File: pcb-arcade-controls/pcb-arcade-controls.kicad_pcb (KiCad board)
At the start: 4 copper layers, 38.1 x 57.2 mm, 26 parts, among them J1 USB_C, SW1 SW_Push, U1 STM32F072CBT6, U3 XC6206, U4 USBLC6-2SC6

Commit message: start aan pcb
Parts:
- removed REF** (x6): MX_1.00u_PG151101S11, ScottoKeebs_Scotto:MX_Hotswap_1.00u
- moved C9 16.1 mm to (156.2, 78.9)
- moved R1 16.1 mm to (142.5, 75.1)
- moved SW1 16.1 mm to (147.3, 76.5)
- moved U3 16.1 mm to (156.7, 76.4)
- moved J1 16.1 mm to (153.8, 57.3)
- moved R2 16.1 mm to (151.9, 63.9)
- moved R3 16.1 mm to (155.5, 63.8)
- moved C8 16.1 mm to (157.2, 74.0)
- moved F1 16.1 mm to (157.5, 72.7)
- moved U4 16.1 mm to (153.3, 71.4)
- moved C10 15.8 mm to (155.2, 101.6)
- moved C13 15.8 mm to (158.6, 98.2)
- moved C14 15.8 mm to (151.5, 101.6)
- moved C15 15.8 mm to (150.5, 101.6)
- moved C16 15.8 mm to (156.2, 90.8)
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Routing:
- net /BOOT0: track 34.8 -> 22.6 mm
- net +3.3V: track 71.5 -> 59.4 mm
- net /MCU_D-: track 18.6 -> 7.85 mm
- net /MCU_D+: track 18.6 -> 7.85 mm
- removed copper zone on In1.Cu, net GND
- removed copper zone on In2.Cu, net GND
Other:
- board size 38.1 x 57.2 mm -> 11 x 11 mm

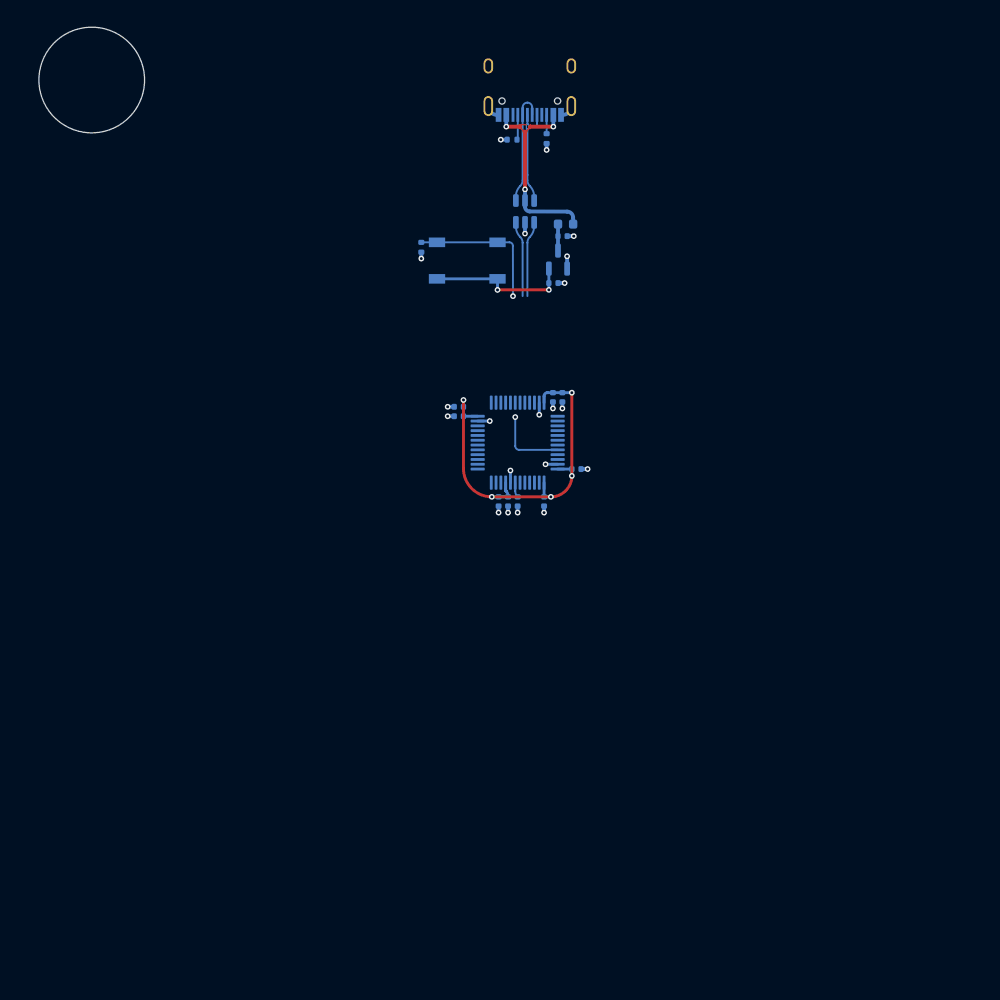
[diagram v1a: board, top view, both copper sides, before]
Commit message: PCB board wipe en connector toevoeging
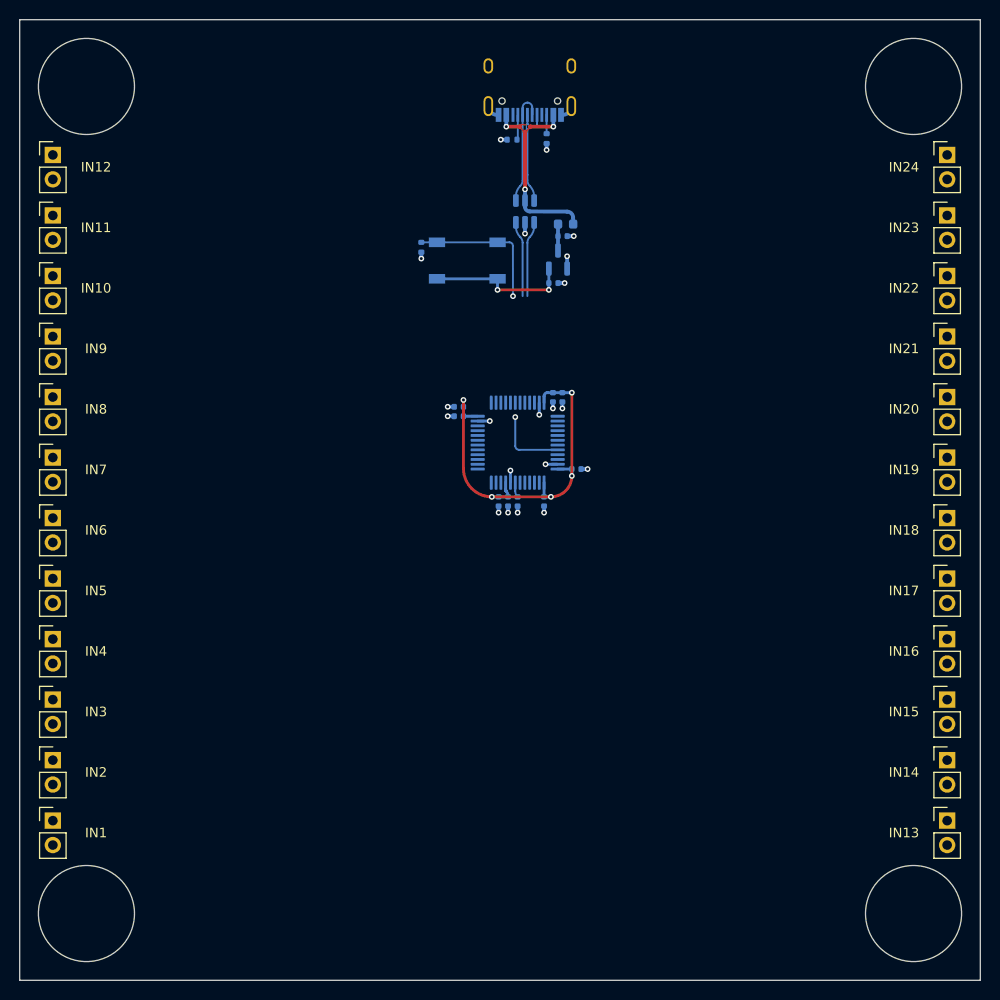
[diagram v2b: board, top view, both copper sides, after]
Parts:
- added H1: 10mm, arcade-controls:MountingHole_10mm, F.Cu at (107.6, 58.4)
- added H2: 10mm, arcade-controls:MountingHole_10mm, F.Cu at (193.7, 58.4)
- added H3: 10mm, arcade-controls:MountingHole_10mm, F.Cu at (107.6, 144.5)
- added H4: 10mm, arcade-controls:MountingHole_10mm, F.Cu at (193.7, 144.5)
- added IN1: Conn_01x02, Connector_PinHeader_2.54mm:PinHeader_1x02_P2.54mm_Vertical, F.Cu at (104.1, 134.8)
- added IN10: Conn_01x02, Connector_PinHeader_2.54mm:PinHeader_1x02_P2.54mm_Vertical, F.Cu at (104.1, 78.1)
- added IN11: Conn_01x02, Connector_PinHeader_2.54mm:PinHeader_1x02_P2.54mm_Vertical, F.Cu at (104.1, 71.8)
- added IN12: Conn_01x02, Connector_PinHeader_2.54mm:PinHeader_1x02_P2.54mm_Vertical, F.Cu at (104.1, 65.5)
- added IN13: Conn_01x02, Connector_PinHeader_2.54mm:PinHeader_1x02_P2.54mm_Vertical, F.Cu at (197.2, 134.8)
- added IN14: Conn_01x02, Connector_PinHeader_2.54mm:PinHeader_1x02_P2.54mm_Vertical, F.Cu at (197.2, 128.5)
- added IN15: Conn_01x02, Connector_PinHeader_2.54mm:PinHeader_1x02_P2.54mm_Vertical, F.Cu at (197.2, 122.2)
- added IN16: Conn_01x02, Connector_PinHeader_2.54mm:PinHeader_1x02_P2.54mm_Vertical, F.Cu at (197.2, 115.9)
- added IN17: Conn_01x02, Connector_PinHeader_2.54mm:PinHeader_1x02_P2.54mm_Vertical, F.Cu at (197.2, 109.6)
- added IN18: Conn_01x02, Connector_PinHeader_2.54mm:PinHeader_1x02_P2.54mm_Vertical, F.Cu at (197.2, 103.3)
- added IN19: Conn_01x02, Connector_PinHeader_2.54mm:PinHeader_1x02_P2.54mm_Vertical, F.Cu at (197.2, 97.0)
- added IN2: Conn_01x02, Connector_PinHeader_2.54mm:PinHeader_1x02_P2.54mm_Vertical, F.Cu at (104.1, 128.5)
- added IN20: Conn_01x02, Connector_PinHeader_2.54mm:PinHeader_1x02_P2.54mm_Vertical, F.Cu at (197.2, 90.7)
- added IN21: Conn_01x02, Connector_PinHeader_2.54mm:PinHeader_1x02_P2.54mm_Vertical, F.Cu at (197.2, 84.4)
- added IN22: Conn_01x02, Connector_PinHeader_2.54mm:PinHeader_1x02_P2.54mm_Vertical, F.Cu at (197.2, 78.1)
- added IN23: Conn_01x02, Connector_PinHeader_2.54mm:PinHeader_1x02_P2.54mm_Vertical, F.Cu at (197.2, 71.8)
- added IN24: Conn_01x02, Connector_PinHeader_2.54mm:PinHeader_1x02_P2.54mm_Vertical, F.Cu at (197.2, 65.5)
- added IN3: Conn_01x02, Connector_PinHeader_2.54mm:PinHeader_1x02_P2.54mm_Vertical, F.Cu at (104.1, 122.2)
- added IN4: Conn_01x02, Connector_PinHeader_2.54mm:PinHeader_1x02_P2.54mm_Vertical, F.Cu at (104.1, 115.9)
- added IN5: Conn_01x02, Connector_PinHeader_2.54mm:PinHeader_1x02_P2.54mm_Vertical, F.Cu at (104.1, 109.6)
- added IN6: Conn_01x02, Connector_PinHeader_2.54mm:PinHeader_1x02_P2.54mm_Vertical, F.Cu at (104.1, 103.3)
- added IN7: Conn_01x02, Connector_PinHeader_2.54mm:PinHeader_1x02_P2.54mm_Vertical, F.Cu at (104.1, 97.0)
- added IN8: Conn_01x02, Connector_PinHeader_2.54mm:PinHeader_1x02_P2.54mm_Vertical, F.Cu at (104.1, 90.7)
- added IN9: Conn_01x02, Connector_PinHeader_2.54mm:PinHeader_1x02_P2.54mm_Vertical, F.Cu at (104.1, 84.4)
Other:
- board size 11 x 11 mm -> 100 x 100 mm
